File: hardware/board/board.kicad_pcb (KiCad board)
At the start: 2 copper layers, 40.1 x 49.3 mm, 54 parts, among them J1 Eurorack Power, Q1 MMBT3904, U1 ATSAMD21G18A-AUT, U2 LM7805, U3 AP2112K-3.3, U4 LM4040DBZ-10, U5 TL072, U6 MCP6001-OT, U7 74AHCT1G125, U8 GD25Q64C

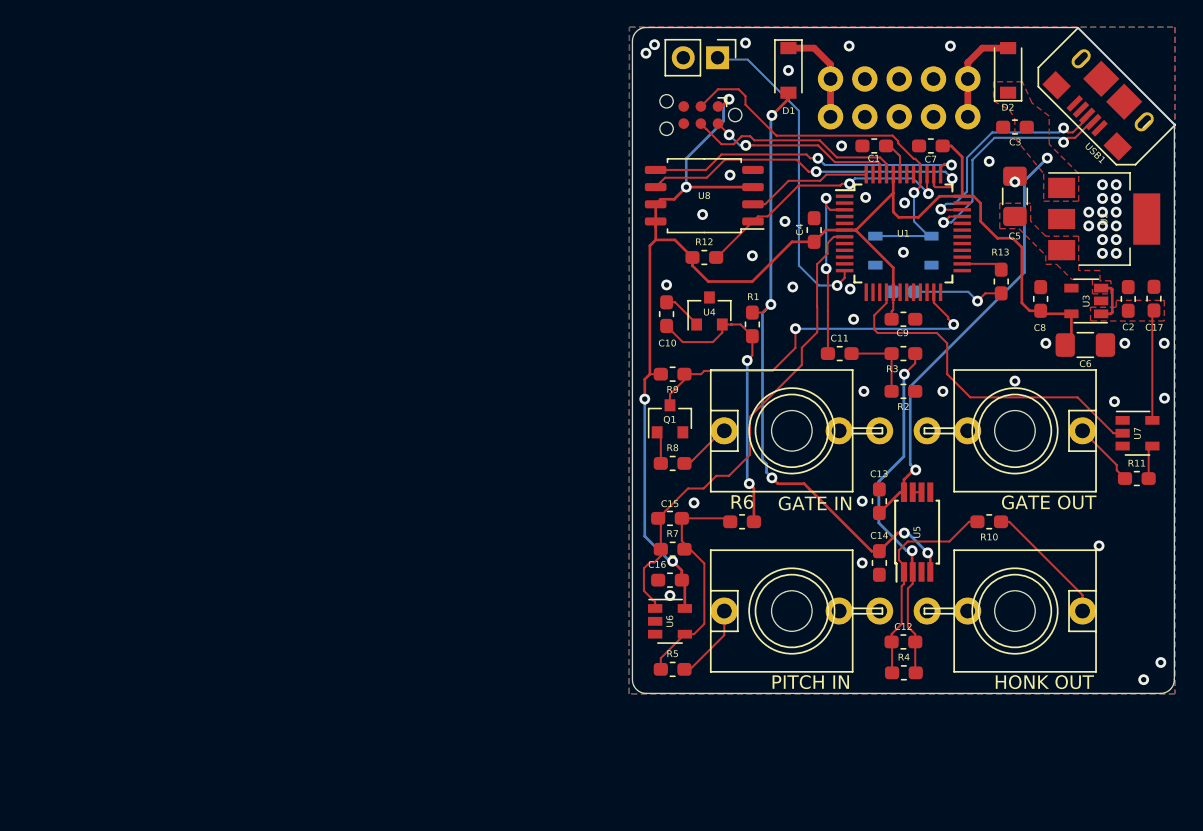
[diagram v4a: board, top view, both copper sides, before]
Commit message: hardware: Add initial version of honk2's mainboard and button board
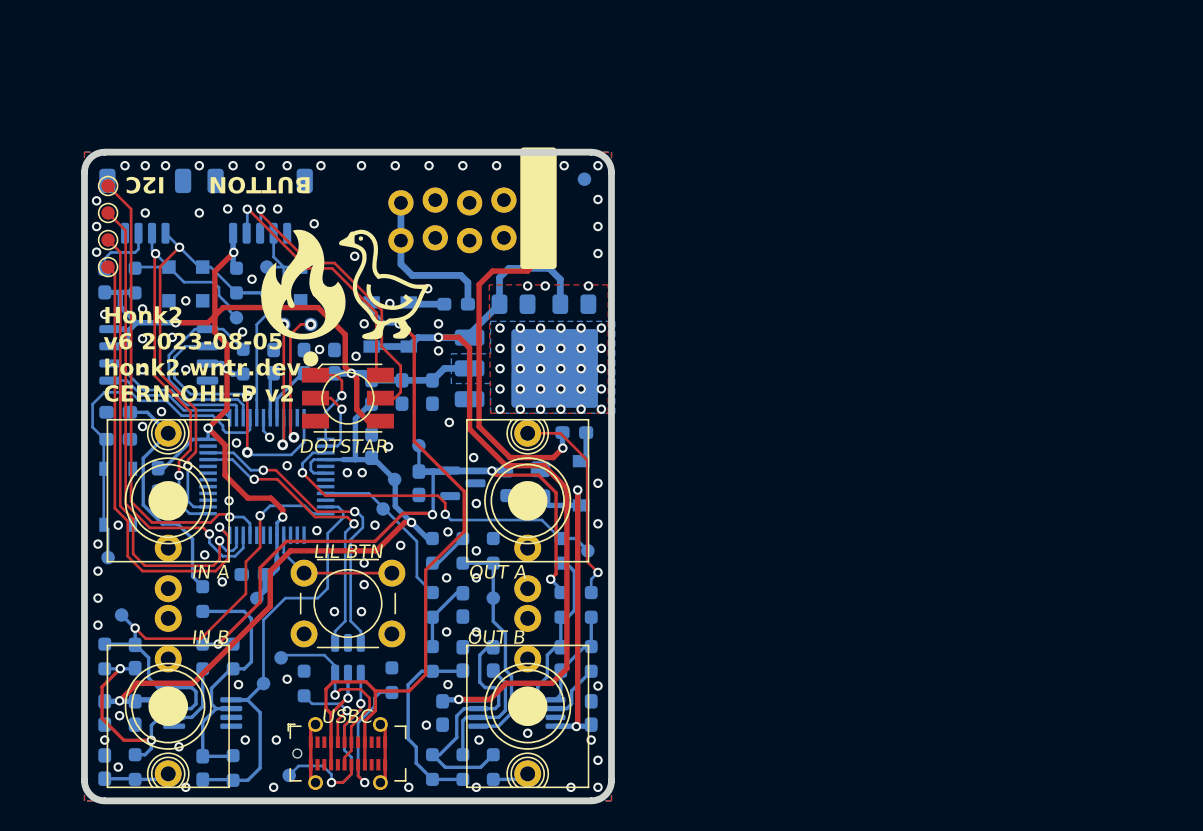
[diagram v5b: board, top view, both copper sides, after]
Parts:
- removed Button1: Big button, Connector_PinHeader_2.54mm:PinHeader_1x02_P2.54mm_Vertical
- removed C3: 1uF, Capacitor_SMD:C_0603_1608Metric_Pad1.05x0.95mm_HandSolder
- removed C4: 0.1uF, Capacitor_SMD:C_0603_1608Metric_Pad1.05x0.95mm_HandSolder
- removed CV_IN1: CV_IN, board:WQP-PJ301M-12_JACK
- removed G***: LOGO, board:winterbloom
- removed G***: LOGO, board:cc_by_sa
- removed GATE_IN1: GATE_IN, board:WQP-PJ301M-12_JACK
- removed GATE_OUT1: GATE_OUT, board:WQP-PJ301M-12_JACK
- removed HONK_OUT1: AUDIO_OUT, board:WQP-PJ301M-12_JACK
- removed Q1: MMBT3904, Package_TO_SOT_SMD:SOT-23
- removed the REF** at (81.5, 144.9)
- removed RESET1: TACT_4.2MM, MF_Switches:MF_Switches-TACT4.2MM
- removed SWD1: Tag-Connect SWD, Connector:Tag-Connect_TC2030-IDC-NL_2x03_P1.27mm_Vertical
- removed U8: GD25Q64C, Package_SO:SOIC-8_5.23x5.23mm_P1.27mm
- removed USB1: USB_MICRO_RIGHT, MF_Connectors:MF_Connectors-MICROUSB-RIGHT
- added ?: , Graphics, F.Cu at (58.9, 118.0)
- added ?: , Graphics, F.Cu at (52.9, 118.0)
- added C18: 100n, winterbloom:C_0603_HandSolder, B.Cu at (40.5, 149.7)
- added C19: 1u, winterbloom:C_0603_HandSolder, B.Cu at (38.2, 149.7)
- added C20: 100n, winterbloom:C_0603_HandSolder, B.Cu at (74.2, 149.7)
- added C21: 100n, winterbloom:C_0603_HandSolder, B.Cu at (63.2, 149.7)
- added C22: 18p, winterbloom:C_0603_HandSolder, B.Cu at (72.0, 145.7)
- added C23: 33n, winterbloom:C_0603_HandSolder, B.Cu at (64.7, 141.7)
- added C24: 1n, winterbloom:C_0603_HandSolder, B.Cu at (64.7, 145.7)
- added C25: 100p, winterbloom:C_0603_HandSolder, B.Cu at (67.0, 145.7)
- added D4: ESD, winterbloom:C_0603_HandSolder, B.Cu at (39.2, 127.4)
- added D5: ESD, winterbloom:C_0603_HandSolder, B.Cu at (38.2, 153.7)
- added D6: Dotstar, winterbloom:LED_APA102_Dotstar_5050, F.Cu at (56.2, 126.4)
- added D7: PESD3V3, winterbloom:D_SOD-323, B.Cu at (43.0, 117.9)
- added D8: PESD3V3, winterbloom:D_SOD-323, B.Cu at (45.5, 117.9)
- added D9: PESD3V3, winterbloom:D_SOD-323, B.Cu at (52.7, 117.9)
- added FB1: 600R@100MHz, winterbloom:L_0603_HandSolder, B.Cu at (64.2, 119.4)
- added FB2: 600R@100MHz, winterbloom:L_0603_HandSolder, B.Cu at (73.0, 128.9)
- added FB3: 600R@100MHz, winterbloom:L_0603_HandSolder, B.Cu at (58.0, 125.9)
- added FB4: 600R@100MHz, winterbloom:L_0603_HandSolder, B.Cu at (38.2, 117.7)
- added J2: Analog In A, winterbloom:AudioJack_WQP518MA, F.Cu at (42.9, 134.0)
- added J3: Analog In B, winterbloom:AudioJack_WQP518MA, F.Cu at (42.9, 149.2)
- added J4: OUT A, winterbloom:AudioJack_WQP518MA, F.Cu at (69.5, 134.0)
- added J5: OUT B, winterbloom:AudioJack_WQP518MA, F.Cu at (69.5, 149.2)
- added J6: USB C/USB 2.0, Connector_USB:USB_C_Receptacle_GCT_USB4115-03-C, F.Cu at (56.2, 152.7)
- added J7: Big button, Connector_JST:JST_SH_SM05B-SRSS-TB_1x05-1MP_P1.00mm_Horizontal, B.Cu at (49.7, 112.2)
- added J9: Qwiic, winterbloom:JST_SH_SM04B-SRSS-TB_1x04-1MP_P1.00mm_Horizontal, B.Cu at (41.2, 112.2)
- added R14: 1k, winterbloom:R_0603_HandSolder, B.Cu at (74.2, 141.7)
- added R15: 1k, winterbloom:R_0603_HandSolder, B.Cu at (62.5, 141.7)
- added R16: 47k, winterbloom:R_0603_HandSolder, B.Cu at (62.5, 145.7)
- added R17: 150k, winterbloom:R_0603_HandSolder, B.Cu at (62.5, 153.7)
- added R18: 150k, winterbloom:R_0603_HandSolder, B.Cu at (64.8, 153.7)
- added R19: 1k, winterbloom:R_0603_HandSolder, B.Cu at (67.0, 153.7)
- added R20: 150k, winterbloom:R_0603_HandSolder, B.Cu at (62.5, 137.7)
- added R21: 10k, winterbloom:R_0603_HandSolder, B.Cu at (64.7, 137.7)
- added R22: 100k, winterbloom:R_0603_HandSolder, B.Cu at (67.0, 137.7)
- added R23: 5k1, winterbloom:R_0603_HandSolder, B.Cu at (53.0, 147.5)
- added R24: 5k1, winterbloom:R_0603_HandSolder, B.Cu at (59.5, 147.2)
- added REF**: OSHW-Logo_5.7x6mm_SilkScreen, Symbol:OSHW-Logo_5.7x6mm_SilkScreen, B.Cu at (56.3, 140.5)
- added SW1: RESET, winterbloom:Tactile_Switch_4.2mm, B.Cu at (39.2, 133.7)
- added SW2: Panel button, winterbloom:Tactile_Switch_6mm, F.Cu at (56.2, 141.6)
- added TP1: GND, TestPoint:TestPoint_Pad_D1.0mm, B.Cu at (73.7, 110.2)
- added TP10: Input A scaled, TestPoint:TestPoint_Pad_D1.0mm, B.Cu at (50.0, 147.5)
- added TP11: Input B scaled, TestPoint:TestPoint_Pad_D1.0mm, B.Cu at (39.5, 142.4)
- added TP12: DAC, TestPoint:TestPoint_Pad_D1.0mm, B.Cu at (74.0, 137.7)
- added TP13: PWM, TestPoint:TestPoint_Pad_D1.0mm, B.Cu at (58.8, 134.6)
- added TP14: 1.25V, TestPoint:TestPoint_Pad_D1.0mm, B.Cu at (67.0, 141.2)
- added TP15: D-, TestPoint:TestPoint_Pad_D1.0mm, B.Cu at (51.3, 145.6)
- added TP16: D+, TestPoint:TestPoint_Pad_D1.0mm, B.Cu at (51.9, 154.3)
- added TP17: BTN, TestPoint:TestPoint_Pad_D1.0mm, B.Cu at (50.2, 116.7)
- added TP18: PA12, TestPoint:TestPoint_Pad_D1.0mm, F.Cu at (38.5, 110.7)
- added TP19: PA13, TestPoint:TestPoint_Pad_D1.0mm, F.Cu at (38.5, 112.7)
- added TP2: 3V3, TestPoint:TestPoint_Pad_D1.0mm, B.Cu at (49.5, 141.2)
- added TP20: PA13, TestPoint:TestPoint_Pad_D1.0mm, F.Cu at (38.5, 114.7)
- added TP21: PA15, TestPoint:TestPoint_Pad_D1.0mm, F.Cu at (38.5, 116.7)
- added TP3: 3V3A, TestPoint:TestPoint_Pad_D1.0mm, B.Cu at (59.7, 132.4)
- added TP4: -10V, TestPoint:TestPoint_Pad_D1.0mm, B.Cu at (61.5, 129.9)
- added TP5: SDA, TestPoint:TestPoint_Pad_D1.0mm, B.Cu at (48.0, 120.4)
- added TP6: SCL, TestPoint:TestPoint_Pad_D1.0mm, B.Cu at (50.2, 118.7)
- added TP7: SWCLK, TestPoint:TestPoint_Pad_D1.0mm, B.Cu at (51.5, 120.9)
- added TP8: SWDIO, TestPoint:TestPoint_Pad_D1.0mm, B.Cu at (53.5, 120.9)
- added TP9: RESET, TestPoint:TestPoint_Pad_D1.0mm, B.Cu at (38.5, 138.2)
- C1, C2: value 1uF -> 22u; footprint Capacitor_SMD:C_0603_1608Metric_Pad1.05x0.95mm_HandSolder -> winterbloom:C_0805_HandSolder; moved to B.Cu
- C10, C13, C7: value 0.1uF -> 100n; footprint Capacitor_SMD:C_0603_1608Metric_Pad1.05x0.95mm_HandSolder -> winterbloom:C_0603_HandSolder; moved to B.Cu
- C11, C8: value 1uF -> 100n; footprint Capacitor_SMD:C_0603_1608Metric_Pad1.05x0.95mm_HandSolder -> winterbloom:C_0603_HandSolder; moved to B.Cu
- C12, C15: value 18pF -> 100n; footprint Capacitor_SMD:C_0603_1608Metric_Pad1.05x0.95mm_HandSolder -> winterbloom:C_0603_HandSolder; moved to B.Cu
- C14, C9: value 0.1uF -> 1u; footprint Capacitor_SMD:C_0603_1608Metric_Pad1.05x0.95mm_HandSolder -> winterbloom:C_0603_HandSolder; moved to B.Cu
- C16: value 0.1uF -> TDB; footprint Capacitor_SMD:C_0603_1608Metric_Pad1.05x0.95mm_HandSolder -> winterbloom:C_0603_HandSolder; moved to B.Cu
- C17: value 1uF -> TBD; footprint Capacitor_SMD:C_0603_1608Metric_Pad1.05x0.95mm_HandSolder -> winterbloom:C_0603_HandSolder; moved to B.Cu
- C5: value 10uF -> 22u; footprint Capacitor_SMD:C_1206_3216Metric_Pad1.42x1.75mm_HandSolder -> winterbloom:C_0805_HandSolder; moved to B.Cu
- C6: value 10uF -> 10u; footprint Capacitor_SMD:C_1206_3216Metric_Pad1.42x1.75mm_HandSolder -> winterbloom:C_0603_HandSolder; moved to B.Cu
- D1, D2: value D -> 30V; footprint Diode_SMD:D_SOD-123 -> winterbloom:D_SOD-123; moved to B.Cu
- D3: value LED -> 30V; footprint Diode_SMD:D_0603_1608Metric -> winterbloom:D_SOD-123
- J1: footprint SF Connectors:2X5-SHROUDED_LOCK -> winterbloom:Eurorack_Power_2x5_Shrouded_Lock
- R1: value 2.2k -> 2k2; footprint Resistor_SMD:R_0603_1608Metric_Pad1.05x0.95mm_HandSolder -> winterbloom:R_0603_HandSolder; moved to B.Cu
- R10: value 1k -> TBD; footprint Resistor_SMD:R_0603_1608Metric_Pad1.05x0.95mm_HandSolder -> winterbloom:R_0603_HandSolder; moved to B.Cu
- R11: value 1k -> 20k; footprint Resistor_SMD:R_0603_1608Metric_Pad1.05x0.95mm_HandSolder -> winterbloom:R_0603_HandSolder; moved to B.Cu
- R12: value 10k -> 3k3; footprint Resistor_SMD:R_0603_1608Metric_Pad1.05x0.95mm_HandSolder -> winterbloom:R_0603_HandSolder; moved to B.Cu
- R13: value 1k -> 10k; footprint Resistor_SMD:R_0603_1608Metric_Pad1.05x0.95mm_HandSolder -> winterbloom:R_0603_HandSolder; moved to B.Cu
- R2: value 47k -> 4k7; footprint Resistor_SMD:R_0603_1608Metric_Pad1.05x0.95mm_HandSolder -> winterbloom:R_0603_HandSolder; moved to B.Cu
- R3: value 6.8k -> 4k7; footprint Resistor_SMD:R_0603_1608Metric_Pad1.05x0.95mm_HandSolder -> winterbloom:R_0603_HandSolder; moved to B.Cu
- R4: value 47k -> 10k; footprint Resistor_SMD:R_0603_1608Metric_Pad1.05x0.95mm_HandSolder -> winterbloom:R_0603_HandSolder; moved to B.Cu
- R5, R8: footprint Resistor_SMD:R_0603_1608Metric_Pad1.05x0.95mm_HandSolder -> winterbloom:R_0603_HandSolder; moved to B.Cu
- R6: value 200k -> TBD; footprint Resistor_SMD:R_0603_1608Metric_Pad1.05x0.95mm_HandSolder -> winterbloom:R_0603_HandSolder; moved to B.Cu
- R7: value 33k -> 61k9; footprint Resistor_SMD:R_0603_1608Metric_Pad1.05x0.95mm_HandSolder -> winterbloom:R_0603_HandSolder; moved to B.Cu
- R9: value 10k -> TBD; footprint Resistor_SMD:R_0603_1608Metric_Pad1.05x0.95mm_HandSolder -> winterbloom:R_0603_HandSolder; moved to B.Cu
- U1: value ATSAMD21G18A-AUT -> LD1117-3.3; footprint Package_QFP:TQFP-48_7x7mm_P0.5mm -> Package_TO_SOT_SMD:TO-252-3_TabPin2; moved to B.Cu
- U2: value LM7805 -> LM4040DBZ-10; footprint Package_TO_SOT_SMD:SOT-223-3_TabPin2 -> Package_TO_SOT_SMD:SOT-23; moved to B.Cu
- U3: value AP2112K-3.3 -> ATSAMD21G18A-A; footprint Package_TO_SOT_SMD:SOT-23-5 -> winterbloom:TQFP-48_7x7mm_P0.5mm; moved to B.Cu
- U4: value LM4040DBZ-10 -> GD25Q64C; footprint Package_TO_SOT_SMD:SOT-23 -> Package_SO:SOIC-8_5.23x5.23mm_P1.27mm; moved to B.Cu
- U5: value TL072 -> MCP6002; footprint Package_SO:TSSOP-8_4.4x3mm_P0.65mm -> Package_SO:MSOP-8_3x3mm_P0.65mm; moved to B.Cu
- U6: value MCP6001-OT -> TL072; footprint Package_TO_SOT_SMD:SOT-23-5 -> Package_SO:TSSOP-8_4.4x3mm_P0.65mm; moved to B.Cu
- U7: value 74AHCT1G125 -> USBLC6-2SC6; footprint Package_TO_SOT_SMD:SOT-23-5 -> Package_TO_SOT_SMD:SOT-23-6; moved to B.Cu
- moved C17 79.9 mm to (40.5, 145.5)
- moved R10 66.2 mm to (38.2, 145.5), turned to -90 degrees
- moved U3 62.0 mm to (50.2, 132.2)
- moved U7 60.8 mm to (56.2, 145.6), turned to -90 degrees
- moved R2 57.4 mm to (40.5, 117.7), turned to 90 degrees
- moved C12 56.4 mm to (42.2, 132.4), turned to -90 degrees
- moved U5 54.5 mm to (45.5, 149.7), turned to 180 degrees
- moved R4 54.0 mm to (48.5, 123.7), turned to 90 degrees
- moved C11 53.8 mm to (39.2, 129.4)
- moved U2 51.3 mm to (64.7, 132.7)
- moved C6 50.7 mm to (60.2, 125.9), turned to -90 degrees
- moved R3 49.6 mm to (48.0, 117.7), turned to -90 degrees
- moved C8 48.0 mm to (61.5, 132.7), turned to -90 degrees
- moved C14 47.2 mm to (50.7, 123.7)
- moved C13 46.6 mm to (49.2, 139.4), turned to 180 degrees
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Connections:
- C1 pad 1: GND -> -12V
- C1 pad 2: Net-(C1-Pad2) -> GND
- C10 pad 1: VREF_-10 -> +3V3
- C11 pad 1: A0 -> /MCU/RESET
- C11 pad 2: Net-(C11-Pad2) -> GND
- C12 pad 1: Net-(C12-Pad1) -> +3V3
- C12 pad 2: Net-(C12-Pad2) -> GND
- C13 pad 1: GND -> +3V3
- C13 pad 2: +12V -> GND
- C14 pad 1: -12V -> GND
- C14 pad 2: GND -> /MCU/VDDCORE
- C15 pad 1: A1 -> +3.3VA
- C15 pad 2: Net-(C15-Pad2) -> GND
- C16 pad 1: +3V3 -> Net-(U5A--)
- C16 pad 2: GND -> /Analog Inputs/ANALOG_IN_A
- C17 pad 1: +5V -> Net-(U5B--)
- C17 pad 2: GND -> /Analog Inputs/ANALOG_IN_B
- C2 pad 1: +5V -> +12V
- C5 pad 1: +5V -> +12V
- C8 pad 1: +3V3 -> VREF-10
- D1 pad 1: Net-(D1-Pad1) -> +12V
- D1 pad 2: -12V -> Net-(D1-A)
- D2 pad 1: +12V -> Net-(D2-K)
- D2 pad 2: Net-(D2-Pad2) -> -12V
- D3 pad 1: GND -> +12V
- D3 pad 2: Net-(D3-Pad2) -> VBUS
- J1 pad 1: Net-(D1-Pad1) -> Net-(FB2-Pad1)
- J1 pad 10: Net-(D2-Pad2) -> Net-(FB1-Pad1)
- J1 pad 2: Net-(D1-Pad1) -> Net-(FB2-Pad1)
- J1 pad 9: Net-(D2-Pad2) -> Net-(FB1-Pad1)
- R1 pad 1: VREF_-10 -> -12V
- R1 pad 2: -12V -> VREF-10
- R10 pad 1: AUDIO_OUT -> /Analog Inputs/ANALOG_IN_B
- R10 pad 2: Net-(C12-Pad1) -> Net-(U5B--)
- R11 pad 1: GATE_OUT -> Net-(U6A--)
- R11 pad 2: Net-(R11-Pad2) -> VREF-10
- R12 pad 1: +3V3 -> Net-(U6A--)
- R12 pad 2: FLASH_CS -> /Analog Outs/DAC IN
- R13 pad 1: Net-(D3-Pad2) -> Net-(C22-Pad1)
- R13 pad 2: D13 -> Net-(U6A--)
- R2 pad 1: GND -> +3V3
- R2 pad 2: Net-(C11-Pad2) -> /MCU/I2C_SDA
- R3 pad 1: Net-(C12-Pad2) -> +3V3
- R3 pad 2: Net-(C11-Pad2) -> /MCU/I2C_SCL
- R4 pad 1: Net-(C12-Pad2) -> +3V3
- R4 pad 2: Net-(C12-Pad1) -> /MCU/FLASH_CS
- R5 pad 1: Net-(C15-Pad2) -> Net-(U5A--)
- R5 pad 2: CV_IN -> /Analog Inputs/ANALOG_IN_A_JACK
- R6 pad 1: Net-(C15-Pad2) -> Net-(U5A--)
- R6 pad 2: VREF_-10 -> VREF-10
- R7 pad 1: A1 -> /Analog Inputs/ANALOG_IN_A
- R7 pad 2: Net-(C15-Pad2) -> Net-(U5A--)
- R8 pad 1: Net-(Q1-Pad1) -> Net-(U5B--)
- R8 pad 2: GATE_IN -> /Analog Inputs/ANALOG_IN_B_JACK
- R9 pad 1: D2 -> Net-(U5B--)
- R9 pad 2: +3V3 -> VREF-10
- U1 pad 1: Net-(U1-Pad1) -> GND
- U1 pad 2: Net-(U1-Pad2) -> +3V3
- U1 pad 3: A0 -> +12V
- U2 pad 1: +12V -> GND
- U2 pad 2: GND -> VREF-10
- U2 pad 3: +5V -> unconnected-(U2-NC-Pad3)
- U3 pad 1: +5V -> /Connectors & buttons/DOTSTAR_DATA
- U3 pad 2: GND -> /Connectors & buttons/DOTSTAR_CLK
- U3 pad 3: +5V -> /Analog Outs/DAC IN
- U3 pad 4: Net-(U3-Pad4) -> +3.3VA
- U3 pad 5: +3V3 -> GND
- U4 pad 1: GND -> /MCU/FLASH_CS
- U4 pad 2: VREF_-10 -> /MCU/FLASH_MISO
- U4 pad 3: (no net) -> +3V3
- U5 pad 1: Net-(C12-Pad1) -> /Analog Inputs/ANALOG_IN_A
- U5 pad 2: Net-(C12-Pad2) -> Net-(U5A--)
- U5 pad 4: -12V -> GND
- U5 pad 6: Net-(U5-Pad6) -> Net-(U5B--)
- U5 pad 7: Net-(U5-Pad6) -> /Analog Inputs/ANALOG_IN_B
- U5 pad 8: +12V -> +3.3VA
- U6 pad 1: A1 -> Net-(C22-Pad1)
- U6 pad 2: GND -> Net-(U6A--)
- U6 pad 4: Net-(C15-Pad2) -> -12V
- U6 pad 5: +3V3 -> /Analog Outs/VREF_1.25V
- U7 pad 1: GND -> /Connectors & buttons/USB_D-
- U7 pad 2: D0 -> GND
- U7 pad 3: GND -> /Connectors & buttons/USB_D+
- U7 pad 4: Net-(R11-Pad2) -> /Connectors & buttons/CONN_D+
- U7 pad 5: +5V -> VBUS
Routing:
- net VBUS: track 0.00 -> 55.9 mm, vias 0 -> 2
- net +3.3VA: track 0.00 -> 52.4 mm, vias 0 -> 2
- net VREF-10: track 0.00 -> 48.3 mm, vias 0 -> 4
- net A1: track 36.1 -> 0.00 mm
- net /Analog Inputs/ANALOG_IN_B: track 0.00 -> 35.8 mm, vias 0 -> 2
- net Net-(U3-PA14): track 0.00 -> 35.0 mm, vias 0 -> 1
- net /MCU/I2C_SDA: track 0.00 -> 34.9 mm, vias 0 -> 2
- net Net-(U3-PA12): track 0.00 -> 34.9 mm, vias 0 -> 1
- net Net-(U3-PA13): track 0.00 -> 33.9 mm, vias 0 -> 1
- net Net-(U3-PA15): track 0.00 -> 33.9 mm, vias 0 -> 1
- net /Analog Inputs/ANALOG_IN_A: track 0.00 -> 32.1 mm
- net /MCU/I2C_SCL: track 0.00 -> 31.4 mm, vias 0 -> 2
- net +12V: track 32.0 -> 62.0 mm
- net RESET: track 29.8 -> 0.00 mm, vias 1 -> 0
- net Net-(FB2-Pad1): track 0.00 -> 28.5 mm, vias 0 -> 1
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- added copper zone on B.Cu, net +3V3
- added copper zone on F.Cu, net +3V3
- removed copper zone on F.Cu, net +12V
- removed copper zone on F.Cu, net +5V
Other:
- board size 40.1 x 49.3 mm -> 39 x 48 mm
- net class Default removed
- rule pad_to_mask_clearance: 0.051 -> 0.0508
- board text added: "${TITLE} ${REVISION} ${ISSUE_DATE} ${COMMENT3} ${COMMENT2}"
- board text added: "-10V"
- board text added: "1V2"
- board text added: "3V3"
- board text added: "3V3A"
- board text added: "BUTTON"
- board text added: "D+"
- board text added: "D-"
- board text added: "DAC"
- board text added: "DOTSTAR"
- board text added: "I2C"
- board text added: "IN A"
- board text added: "IN B"
- board text added: "In A"
- board text added: "In B"
- board text added: "LIL BTN"
- board text added: "OUT A"
- board text added: "OUT B"
- board text added: "PCB Specifications: - 4 copper layers - Size: 70.8 x 108 mm - Thickness: 1.6 mm - Material: FR4 TG-140+ - Min track width/spacing: 0.153 mm (6 mil) - Min hole size: 0.3 mm - Soldermask: Pink/Purple/Matte Black - Silkscreen: Black/White - Finish: ENIG 2U{dblquote} - Copper: 1 oz - UL Marking: on top silkscreen"
- board text added: "PWM"
- board text added: "RST"
- board text added: "SWD"
- board text added: "USBC"
- board text removed: "Big Honking Button"
- board text removed: "GATE IN"
- board text removed: "GATE OUT"
- board text removed: "HONK OUT"
- board text removed: "PITCH IN"
- board text removed: "RED STRIPE"
- board text removed: "TRANS RIGHTS"
- board text removed: "v5 10/7/2020 CC BY-SA 4.0 wntr.dev/honk"

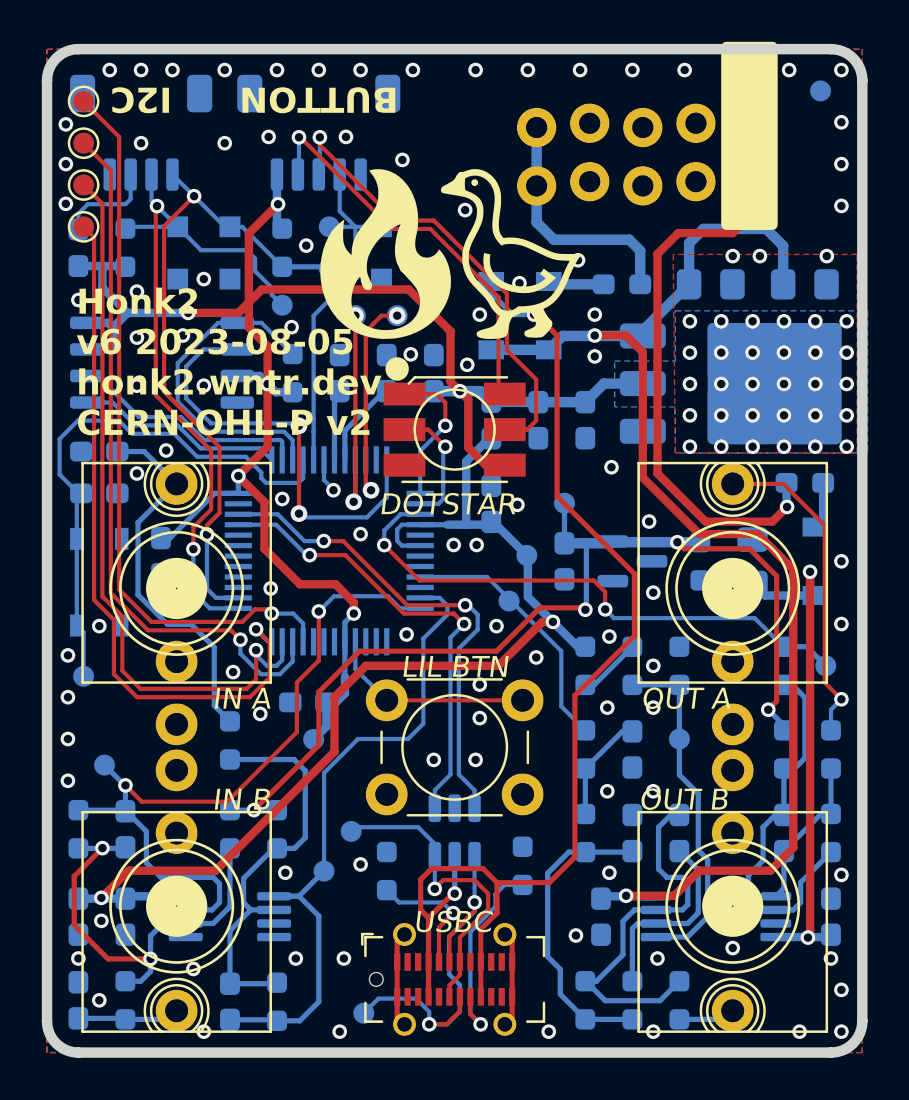
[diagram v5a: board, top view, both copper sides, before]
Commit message: hardware: change USB connector, change flash chip, change SPI flash pin assignments, other small updates to routing
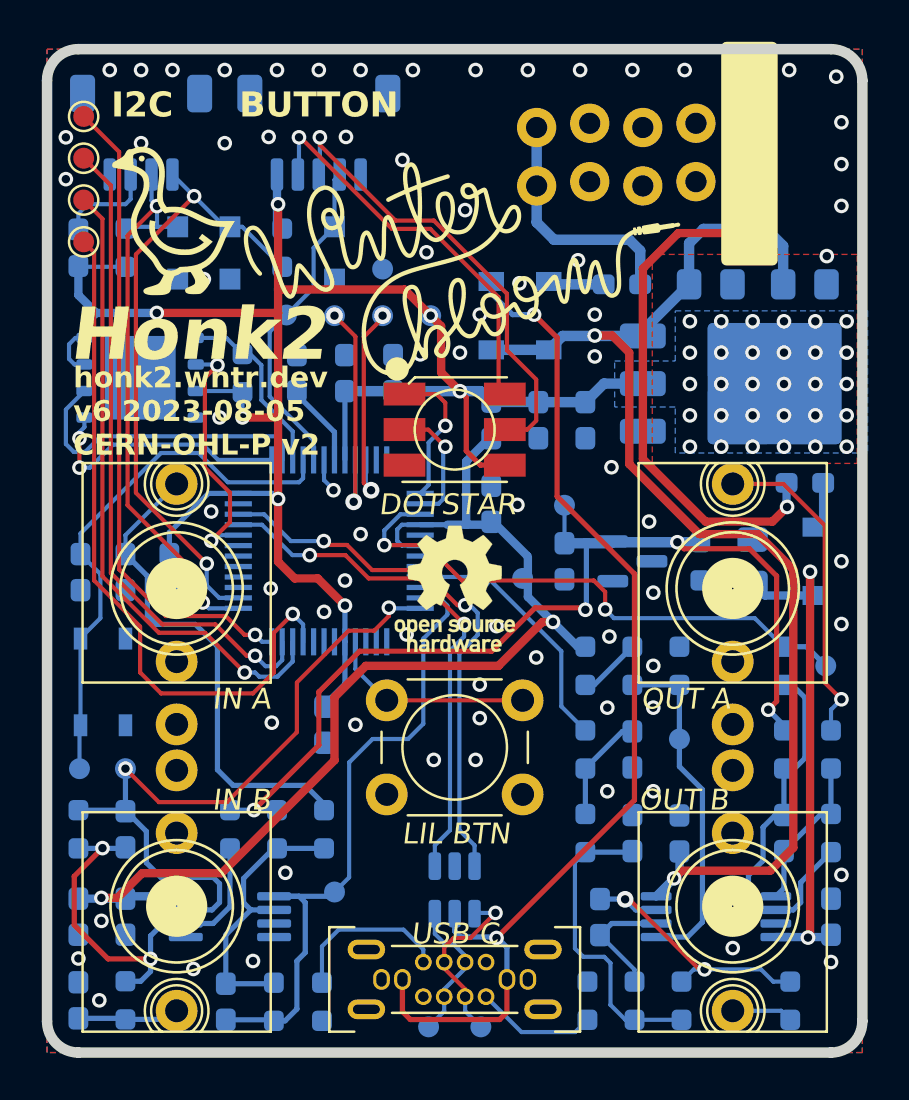
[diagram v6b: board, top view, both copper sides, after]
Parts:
- removed the ? at (58.9, 118.0)
- removed the ? at (52.9, 118.0)
- removed TP5: SDA, TestPoint:TestPoint_Pad_D1.0mm
- removed TP6: SCL, TestPoint:TestPoint_Pad_D1.0mm
- added ?: , Graphics, F.Cu at (42.8, 116.4)
- added G***: LOGO, LOGO, F.Cu at (56.7, 117.4)
- C16: value TDB -> 18pF
- C17: value TBD -> 18pF
- J6: footprint Connector_USB:USB_C_Receptacle_GCT_USB4115-03-C -> winterbloom:USB_C_Vertical_GT-USB-7038X
- R10: value TBD -> 33k
- R6, R9: value TBD -> 200k
- R7: value 61k9 -> 33k
- REF**: moved to F.Cu
- U4: value GD25Q64C -> W25Q64JVZPIQ; footprint Package_SO:SOIC-8_5.23x5.23mm_P1.27mm -> Package_SON:WSON-8-1EP_6x5mm_P1.27mm_EP3.4x4mm
- moved TP1 22.6 mm to (52.8, 118.7)
- moved TP2 21.0 mm to (55.1, 120.9)
- moved TP15 10.1 mm to (55.0, 154.9)
- moved R24 7.16 mm to (62.6, 153.7)
- moved R23 6.98 mm to (49.9, 153.8), turned to -90 degrees
- moved TP18 6.72 mm to (38.5, 117.4)
- moved REF** 6.53 mm to (56.2, 134.0), turned to 0 degrees
- moved R5 6.19 mm to (50.0, 145.5)
- moved D4 5.90 mm to (40.5, 133.2), turned to 90 degrees
- moved TP16 5.64 mm to (57.5, 154.9)
- moved C25 5.53 mm to (63.2, 149.7)
- moved C21 5.47 mm to (67.0, 145.7), turned to 90 degrees
- moved R19 5.30 mm to (72.3, 153.7)
- moved TP21 5.28 mm to (38.5, 111.4)
- moved SW1 4.77 mm to (39.4, 138.4)
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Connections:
- U3 pad 32: unconnected-(U3-PA23-Pad32) -> /MCU/FLASH_MISO
- U3 pad 48: /MCU/FLASH_MISO -> unconnected-(U3-PB03-Pad48)
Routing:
- net /Connectors & buttons/CONN_D+: track 19.9 -> 8.33 mm, vias 2 -> 1
- net GND: track 11.0 -> 1.78 mm, vias 103 -> 77
- net /MCU/FLASH_MISO: track 20.9 -> 12.0 mm
- net /Connectors & buttons/CONN_D-: track 15.0 -> 6.68 mm, vias 1 -> 0
- net /MCU/FLASH_CS: track 16.0 -> 8.46 mm
- net /MCU/I2C_SDA: track 34.9 -> 27.9 mm
- net Net-(U5A--): track 19.5 -> 13.3 mm
- net /Analog Inputs/ANALOG_IN_A_JACK: track 18.1 -> 23.4 mm
- net Net-(C25-Pad1): track 18.5 -> 13.8 mm, vias 0 -> 2
- net VBUS: track 55.9 -> 51.2 mm
- net Net-(J6-CC2): track 9.93 -> 5.80 mm, vias 1 -> 0
- net /MCU/FLASH_SCK: track 11.0 -> 14.7 mm
- net Net-(U3-PA14): track 35.0 -> 31.4 mm
- net Net-(U6B--): track 9.31 -> 5.82 mm
- net Net-(U3-PA13): track 33.9 -> 30.7 mm
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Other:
- board text added: "${COMMENT3} ${REVISION} ${ISSUE_DATE} ${COMMENT2}"
- board text added: "${REVISION}"
- board text added: "${TITLE}"
- board text added: "USB C"
- board text added: "trans rights"
- board text removed: "${TITLE} ${REVISION} ${ISSUE_DATE} ${COMMENT3} ${COMMENT2}"
- board text removed: "-10V"
- board text removed: "1V2"
- board text removed: "3V3"
- board text removed: "3V3A"
- board text removed: "D+"
- board text removed: "D-"
- board text removed: "DAC"
- board text removed: "In A"
- board text removed: "In B"
- board text removed: "PWM"
- board text removed: "RST"
- board text removed: "SWD"
- board text removed: "USBC"

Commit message: hardware: rename to Goosehonk Nebula, prep v7
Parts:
- removed the G*** at (56.7, 117.4)
- added G***: LOGO, winterbloom:Symbol_Winterbloom_25mm, F.Cu at (57.2, 121.5)
- moved ? 13.9 mm to (56.3, 113.2)
- moved REF** 0.28 mm to (56.2, 134.3)
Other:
- board text added: "${COMMENT3} / ${REVISION} ${ISSUE_DATE} / ${COMMENT2}"
- board text added: "Goosehonk Nebula"
- board text removed: "${COMMENT3} ${REVISION} ${ISSUE_DATE} ${COMMENT2}"
- board text removed: "${TITLE}"
